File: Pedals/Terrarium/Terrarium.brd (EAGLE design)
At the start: 59.4 x 57.1 mm, 43 parts, among them IC1 TL072CP, IC2 L78L05CZ, SW1 SPST, SW2 SPST, SW3 SPST, SW4 SPST

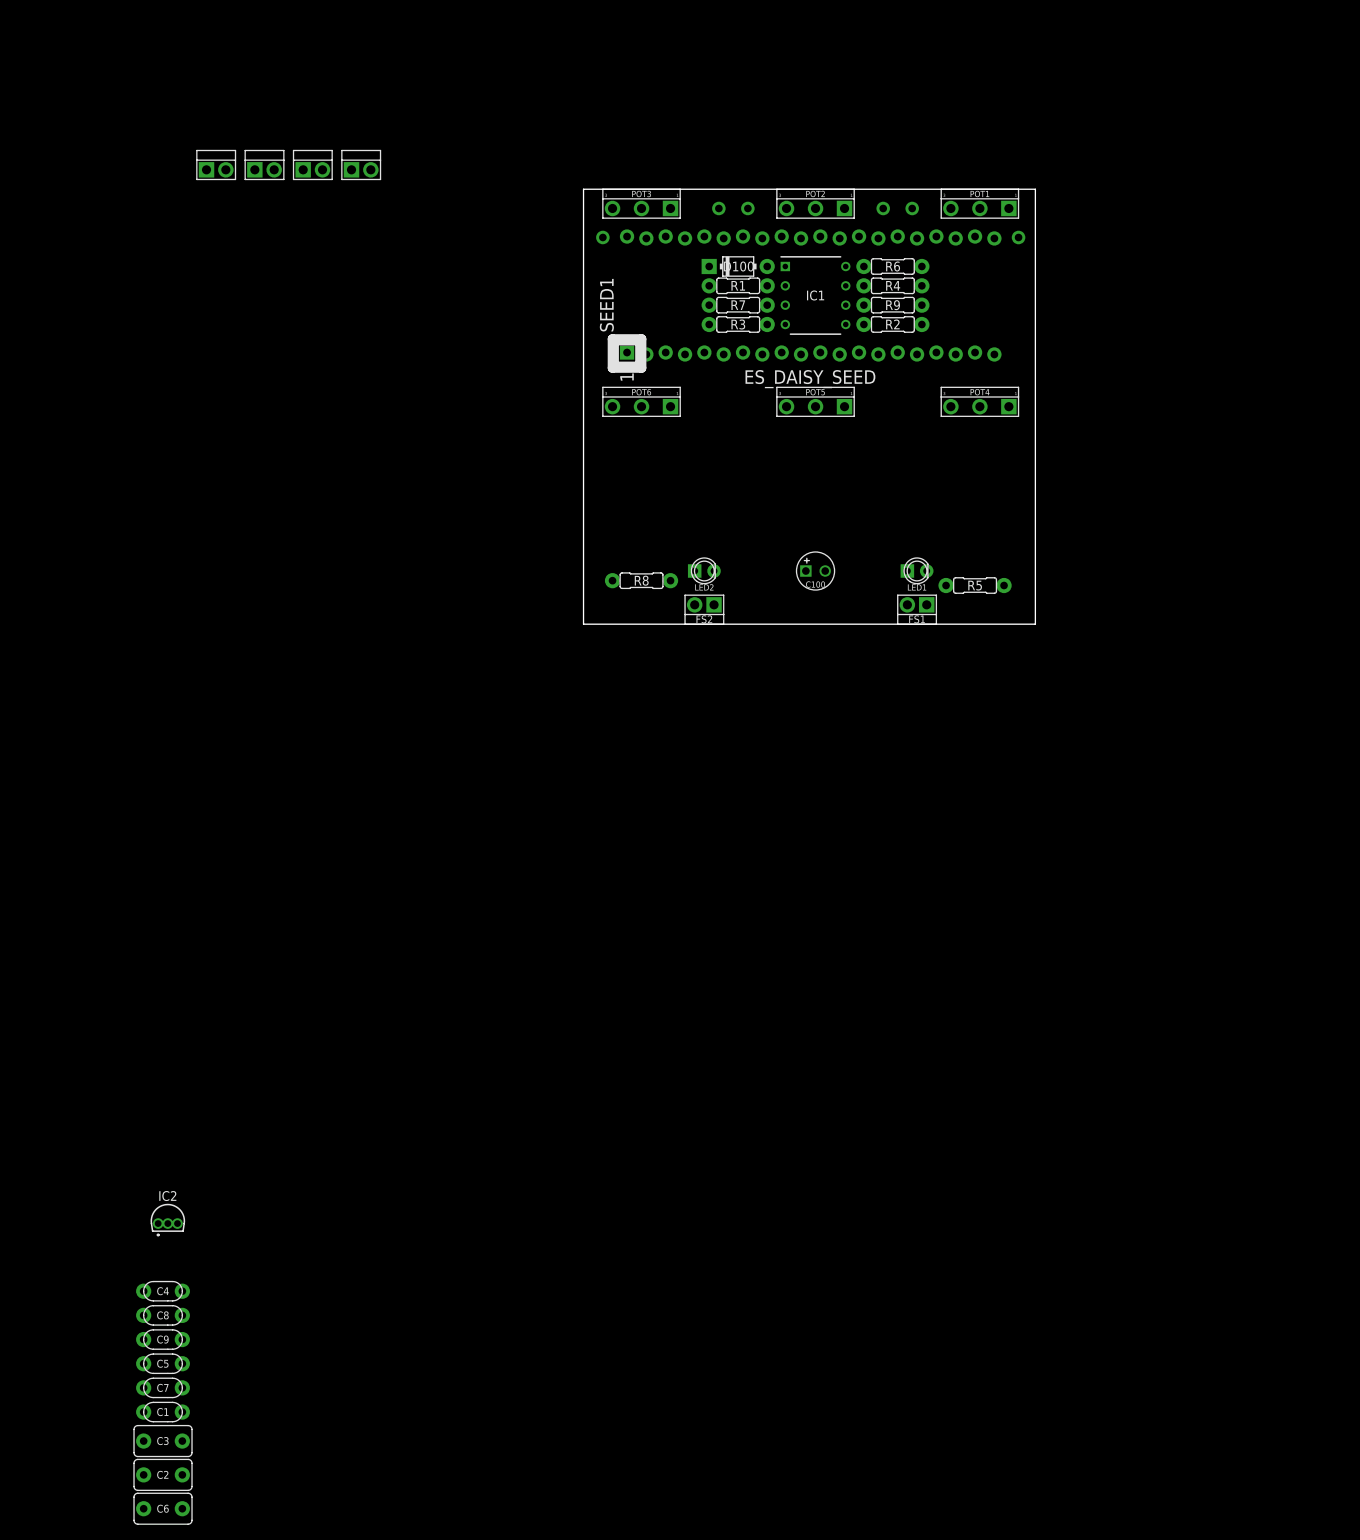
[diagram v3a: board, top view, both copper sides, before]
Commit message: Update parts and place them on the board
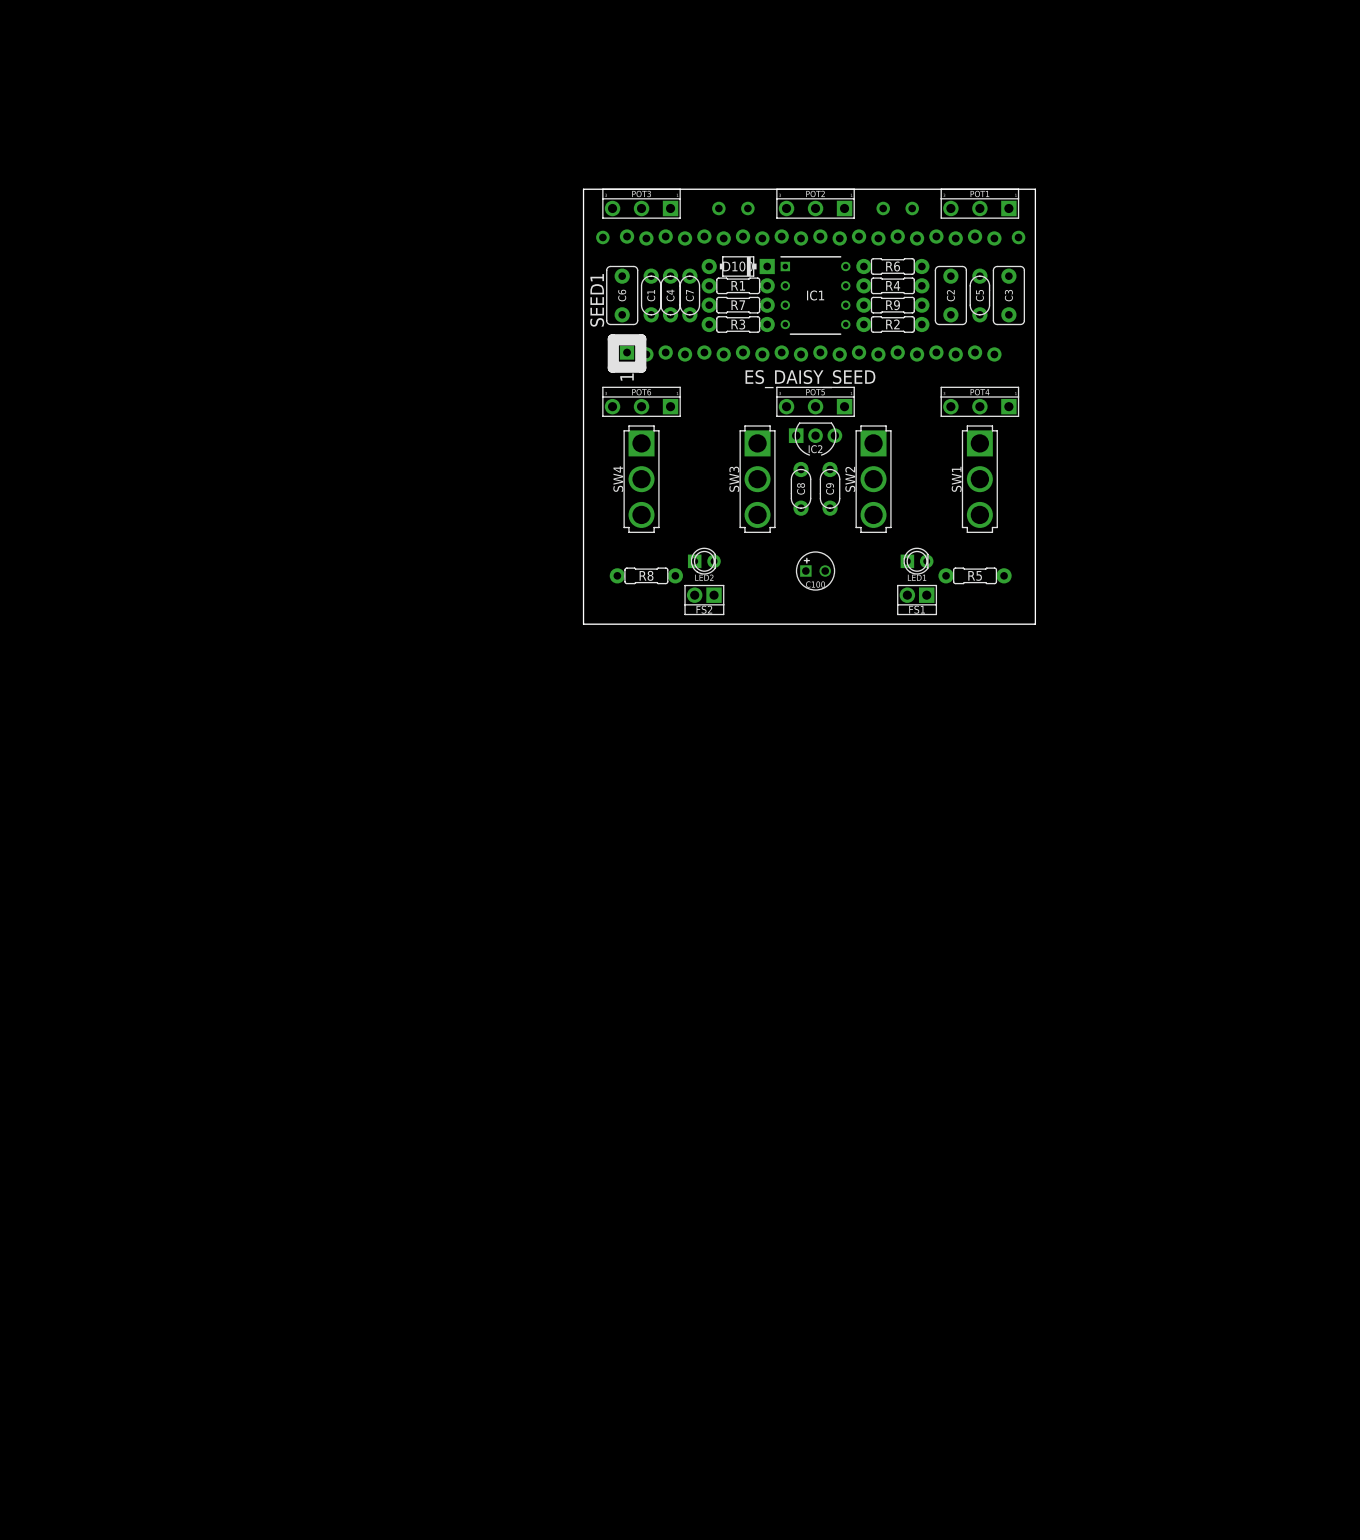
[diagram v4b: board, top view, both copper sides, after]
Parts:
- IC2: value L78L05CZ -> LM78L05; device SamacSys_Parts:TS1107A1AP -> regulators:TO92-
- SW1, SW2, SW3, SW4: value SPST -> (none); device switches:SPST -> switches:SPDT_SOLDER_LUG
- moved C3 187.1 mm to (55.9, 43.2), turned to 90 degrees
- moved C2 186.3 mm to (48.3, 43.2), turned to 90 degrees
- moved C5 176.7 mm to (52.1, 43.2), turned to 90 degrees
- moved C6 170.4 mm to (5.08, 43.2), turned to 270 degrees
- moved C1 160.1 mm to (8.89, 43.2), turned to 90 degrees
- moved C7 159.3 mm to (14.0, 43.2), turned to 90 degrees
- moved C4 146.8 mm to (11.4, 43.2), turned to 270 degrees
- moved C9 142.0 mm to (32.4, 17.8), turned to 270 degrees
- moved C8 137.2 mm to (28.6, 17.8), turned to 270 degrees
- moved IC2 134.8 mm to (30.5, 24.8)
- moved SW1 90.9 mm to (52.1, 19.1), turned to 90 degrees
- moved SW2 84.1 mm to (38.1, 19.1), turned to 90 degrees
- moved SW3 76.5 mm to (22.9, 19.1), turned to 90 degrees
- moved SW4 69.1 mm to (7.62, 19.1), turned to 90 degrees
- moved LED1 1.27 mm to (43.8, 8.26)
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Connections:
- net +5V: now also IC2.3; no longer IC2.1
- net GND: now also SW1.3, SW2.3, SW3.3, SW4.3; no longer SW1.2, SW2.2, SW3.2, SW4.2
- net SW1: now also SW1.2; no longer SW1.1
- net SW2: now also SW2.2; no longer SW2.1
- net SW3: now also SW3.2; no longer SW3.1
- net SW4: now also SW4.2; no longer SW4.1
- net VCC: now also IC2.1; no longer IC2.3

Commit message: Working on routing
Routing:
- net GND: track 0.00 -> 293.1 mm
- net 3V3_A: track 0.00 -> 134.4 mm, vias 0 -> 2
- net +5V: track 0.00 -> 79.5 mm, vias 0 -> 1
- net N$3: track 0.00 -> 46.0 mm, vias 0 -> 1
- net VCC: track 0.00 -> 41.0 mm
- net SW1: track 0.00 -> 36.4 mm
- net N$5: track 0.00 -> 30.8 mm, vias 0 -> 1
- net N$4: track 0.00 -> 28.3 mm, vias 0 -> 2
- net SW2: track 0.00 -> 28.1 mm
- net LEFT_IN: track 0.00 -> 25.7 mm, vias 0 -> 1
- net N$10: track 0.00 -> 24.0 mm, vias 0 -> 2
- net SW4: track 0.00 -> 23.0 mm
- net N$17: track 0.00 -> 19.5 mm
- net N$11: track 0.00 -> 18.0 mm
- net SW3: track 0.00 -> 18.0 mm
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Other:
- board size 59.4 x 57.1 mm -> 59.4 x 57.8 mm

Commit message: Working on routing
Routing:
- net LED1: track 0.00 -> 62.7 mm, vias 0 -> 1
- net N$6: track 0.00 -> 42.8 mm, vias 0 -> 1
- net +5V: track 79.5 -> 78.2 mm
- net N$5: track 30.8 -> 29.5 mm, vias 1 -> 0
- net N$14: track 17.4 -> 16.9 mm
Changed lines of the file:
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@@
 <wire x1="57.785" y1="31.623" x2="53.975" y2="35.433" width="0.3048" layer="16"/>
 <wire x1="57.785" y1="26.67" x2="57.785" y2="31.623" width="0.3048" layer="16"/>
-<wire x1="36.83" y1="46.99" x2="40.005" y2="46.99" width="0.3048" layer="16"/>
-<wire x1="40.005" y1="46.99" x2="42.545" y2="49.53" width="0.3048" layer="16"/>
-<wire x1="42.545" y1="49.53" x2="43.19786875" y2="49.53" width="0.3048" layer="16"/>
+<wire x1="36.83" y1="46.99" x2="37.973" y2="46.99" width="0.3048" layer="16"/>
+<wire x1="37.973" y1="46.99" x2="40.513" y2="49.53" width="0.3048" layer="16"/>
+<wire x1="40.513" y1="49.53" x2="43.19786875" y2="49.53" width="0.3048" layer="16"/>
 <wire x1="43.19786875" y1="49.53" x2="43.29946875" y2="49.4284" width="0.3048" layer="16"/>
 <wire x1="48.3616" y1="49.4284" x2="52.07" y2="45.72" width="0.3048" layer="16"/>
@@
 <contactref element="SEED1" pad="27"/>
 <contactref element="POT5" pad="2"/>
-<wire x1="38.735" y1="50.673" x2="38.735" y2="48.895" width="0.3048" layer="16"/>
-<wire x1="33.14354375" y1="46.99" x2="32.258" y2="46.99" width="0.3048" layer="16"/>
-<wire x1="38.1348" y1="48.2948" x2="34.44834375" y2="48.2948" width="0.3048" layer="16"/>
-<wire x1="34.44834375" y1="48.2948" x2="33.14354375" y2="46.99" width="0.3048" layer="16"/>
-<wire x1="38.735" y1="48.895" x2="38.1348" y2="48.2948" width="0.3048" layer="16"/>
 <wire x1="27.3304" y1="34.91746875" x2="27.3304" y2="35.94853125" width="0.3048" layer="1"/>
 <wire x1="30.48" y1="28.575" x2="30.48" y2="31.76786875" width="0.3048" layer="1"/>
 <wire x1="30.48" y1="31.76786875" x2="27.3304" y2="34.91746875" width="0.3048" layer="1"/>
-<via x="32.258" y="46.99" extent="1-16" drill="0.35"/>
-<wire x1="32.258" y1="40.87613125" x2="32.258" y2="46.99" width="0.3048" layer="1"/>
-<wire x1="27.3304" y1="35.94853125" x2="32.258" y2="40.87613125" width="0.3048" layer="1"/>
+<wire x1="32.258" y1="40.87613125" x2="27.3304" y2="35.94853125" width="0.3048" layer="1"/>
+<wire x1="38.735" y1="50.673" x2="38.735" y2="50.165" width="0.3048" layer="1"/>
+<wire x1="37.322" y1="48.752" x2="34.90554375" y2="48.752" width="0.3048" layer="1"/>
+<wire x1="38.735" y1="50.165" x2="37.322" y2="48.752" width="0.3048" layer="1"/>
+<wire x1="32.258" y1="46.10445625" x2="32.258" y2="40.87613125" width="0.3048" layer="1"/>
+<wire x1="34.90554375" y1="48.752" x2="32.258" y2="46.10445625" width="0.3048" layer="1"/>
 </signal>
 <signal name="N$6">
 <contactref element="SEED1" pad="28"/>
 <contactref element="POT6" pad="2"/>
-<wire x1="7.62" y1="28.575" x2="36.195" y2="50.927" width="0" layer="19" extent="1-1"/>
+<wire x1="36.195" y1="50.927" x2="36.195" y2="49.3362" width="0.3048" layer="1"/>
+<wire x1="36.195" y1="49.3362" x2="36.068" y2="49.2092" width="0.3048" layer="1"/>
+<wire x1="36.068" y1="49.2092" x2="34.7161625" y2="49.2092" width="0.3048" layer="1"/>
+<wire x1="34.7161625" y1="49.2092" x2="31.8008" y2="46.2938375" width="0.3048" layer="1"/>
+<wire x1="31.8008" y1="46.2938375" x2="31.8008" y2="41.1988" width="0.3048" layer="1"/>
+<wire x1="25.51946875" y1="36.9316" x2="24.7904" y2="36.20253125" width="0.3048" layer="1"/>
+<wire x1="27.5336" y1="36.9316" x2="25.51946875" y2="36.9316" width="0.3048" layer="1"/>
+<wire x1="24.7904" y1="36.20253125" x2="24.7904" y2="34.4424" width="0.3048" layer="1"/>
+<wire x1="24.7904" y1="34.4424" x2="22.86" y2="32.512" width="0.3048" layer="1"/>
+<wire x1="31.8008" y1="41.1988" x2="27.5336" y2="36.9316" width="0.3048" layer="1"/>
+<via x="22.86" y="32.512" extent="1-16" drill="0.35"/>
+<wire x1="22.86" y1="32.512" x2="11.557" y2="32.512" width="0.3048" layer="16"/>
+<wire x1="11.557" y1="32.512" x2="7.62" y2="28.575" width="0.3048" layer="16"/>
 </signal>
 <signal name="FS2">
@@
 <contactref element="SEED1" pad="29"/>
 <contactref element="R5" pad="2"/>
-<wire x1="55.245" y1="6.35" x2="33.655" y2="50.673" width="0" layer="19" extent="1-1"/>
+<wire x1="33.655" y1="50.673" x2="35.56" y2="48.768" width="0.3048" layer="16"/>
+<wire x1="35.56" y1="48.768" x2="38.1" y2="48.768" width="0.3048" layer="16"/>
+<wire x1="55.245" y1="6.35" x2="57.658" y2="6.35" width="0.3048" layer="1"/>
+<wire x1="58.1916" y1="6.8836" x2="58.1916" y2="43.434" width="0.3048" layer="1"/>
+<wire x1="57.658" y1="6.35" x2="58.1916" y2="6.8836" width="0.3048" layer="1"/>
+<wire x1="58.1916" y1="43.434" x2="57.4296" y2="44.196" width="0.3048" layer="1"/>
+<wire x1="57.4296" y1="44.196" x2="52.324" y2="44.196" width="0.3048" layer="1"/>
+<via x="52.324" y="44.196" extent="1-16" drill="0.35"/>
+<wire x1="52.324" y1="44.196" x2="52.1048" y2="44.4152" width="0.3048" layer="16"/>
+<wire x1="52.1048" y1="44.4152" x2="51.52953125" y2="44.4152" width="0.3048" layer="16"/>
+<wire x1="51.52953125" y1="44.4152" x2="50.7652" y2="45.17953125" width="0.3048" layer="16"/>
+<wire x1="50.7652" y1="45.17953125" x2="50.7652" y2="46.37821875" width="0.3048" layer="16"/>
+<wire x1="48.17221875" y1="48.9712" x2="43.434" y2="48.9712" width="0.3048" layer="16"/>
+<wire x1="50.7652" y1="46.37821875" x2="48.17221875" y2="48.9712" width="0.3048" layer="16"/>
+<wire x1="43.434" y1="48.9712" x2="38.1" y2="48.768" width="0" layer="19" extent="16-16"/>
 </signal>
 <signal name="LEFT_OUT">
@@
 <wire x1="33.18" y1="45.72" x2="34.45" y2="46.99" width="0.4064" layer="16"/>
 <wire x1="25.4" y1="45.72" x2="33.18" y2="45.72" width="0.4064" layer="16"/>
-<wire x1="36.83" y1="39.37" x2="35.56" y2="40.64" width="0.4064" layer="1"/>
-<wire x1="35.56" y1="40.64" x2="33.02" y2="40.64" width="0.4064" layer="1"/>
-<wire x1="33.02" y1="40.64" x2="33.02" y2="45.72" width="0.4064" layer="1"/>
-<wire x1="33.02" y1="45.72" x2="34.29" y2="46.99" width="0.4064" layer="1"/>
-<wire x1="34.29" y1="46.99" x2="34.45" y2="46.99" width="0.4064" layer="1"/>
 <wire x1="36.83" y1="39.37" x2="40.64" y2="39.37" width="0.4064" layer="16"/>
 <wire x1="40.64" y1="39.37" x2="42.545" y2="37.465" width="0.4064" layer="16"/>
@@
 <wire x1="52.705" y1="33.655" x2="52.705" y2="40.005" width="0.3048" layer="16"/>
 <wire x1="52.705" y1="40.005" x2="52.07" y2="40.64" width="0.3048" layer="16"/>
+<wire x1="33.5262" y1="41.52734375" x2="34.06734375" y2="40.9862" width="0.3048" layer="1"/>
+<wire x1="34.45" y1="46.99" x2="34.45" y2="45.75645625" width="0.3048" layer="1"/>
+<wire x1="35.2138" y1="40.9862" x2="36.83" y2="39.37" width="0.3048" layer="1"/>
+<wire x1="34.45" y1="45.75645625" x2="33.5262" y2="44.83265625" width="0.3048" layer="1"/>
+<wire x1="34.06734375" y1="40.9862" x2="35.2138" y2="40.9862" width="0.3048" layer="1"/>
+<wire x1="33.5262" y1="44.83265625" x2="33.5262" y2="41.52734375" width="0.3048" layer="1"/>
 </signal>
 <signal name="N$10">
 <contactref element="R4" pad="1"/>
 <contactref element="C3" pad="1"/>
-<wire x1="36.83" y1="44.45" x2="42.545" y2="38.735" width="0.3048" layer="1"/>
-<via x="42.545" y="38.735" extent="1-16" drill="0.35"/>
+<wire x1="36.83" y1="44.45" x2="38.989" y2="42.037" width="0.3048" layer="1"/>
+<via x="38.989" y="42.037" extent="1-16" drill="0.35"/>
 <wire x1="43.307" y1="37.973" x2="50.165" y2="37.973" width="0.3048" layer="16"/>
-<wire x1="42.545" y1="38.735" x2="43.307" y2="37.973" width="0.3048" layer="16"/>
+<wire x1="38.989" y1="42.037" x2="43.307" y2="37.973" width="0.3048" layer="16"/>
 <wire x1="50.165" y1="37.973" x2="50.8" y2="38.608" width="0.3048" layer="16"/>
 <wire x1="50.8" y1="38.608" x2="50.8" y2="38.735" width="0.3048" layer="16"/>
@@
 <contactref element="R4" pad="2"/>
 <wire x1="34.45" y1="44.45" x2="34.45" y2="41.91" width="0.4064" layer="1"/>
-<wire x1="35.4744" y1="47.5515125" x2="36.2684875" y2="48.3456" width="0.4064" layer="1"/>
-<wire x1="34.45" y1="44.45" x2="35.4744" y2="45.4744" width="0.4064" layer="1"/>
-<wire x1="36.2684875" y1="48.3456" x2="36.2806" y2="48.3456" width="0.4064" layer="1"/>
-<wire x1="36.2806" y1="48.3456" x2="36.83" y2="48.895" width="0.4064" layer="1"/>
-<wire x1="35.4744" y1="45.4744" x2="35.4744" y2="47.5515125" width="0.4064" layer="1"/>
-<wire x1="36.83" y1="48.895" x2="40.005" y2="48.895" width="0.4064" layer="1"/>
-<wire x1="40.005" y1="48.895" x2="44.45" y2="44.45" width="0.4064" layer="1"/>
+<wire x1="35.5252" y1="47.53046875" x2="36.28953125" y2="48.2948" width="0.3048" layer="1"/>
+<wire x1="36.28953125" y1="48.2948" x2="37.37046875" y2="48.2948" width="0.3048" layer="1"/>
+<wire x1="34.45" y1="44.45" x2="35.5252" y2="45.5252" width="0.3048" layer="1"/>
+<wire x1="35.5252" y1="45.5252" x2="35.5252" y2="47.53046875" width="0.3048" layer="1"/>
+<wire x1="41.21526875" y1="44.45" x2="44.45" y2="44.45" width="0.3048" layer="1"/>
+<wire x1="37.37046875" y1="48.2948" x2="41.21526875" y2="44.45" width="0.3048" layer="1"/>
 </signal>
 <signal name="N$11">
